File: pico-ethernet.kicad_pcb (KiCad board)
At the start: 2 copper layers, 55 x 22 mm, 28 parts, among them J1 Conn_01x20_Pin, J2 Conn_01x02_Pin, J3 VR05S05, J4 SI-52003-F, J5 Conn_01x02, U1 ENC28J60x-SS, Y1 25MHz

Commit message: interrupt
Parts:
- J2: footprint Connector_PinSocket_2.54mm:PinSocket_1x04_P2.54mm_Vertical -> Connector_PinSocket_2.54mm:PinSocket_1x05_P2.54mm_Vertical
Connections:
- U1 pad 4: unconnected-(U1-~{INT}-Pad4) -> Net-(J2-Pin_5)
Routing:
- net Net-(J2-Pin_5): track 0.00 -> 12.4 mm
- net GND: track 14.2 -> 11.3 mm, vias 4 -> 3

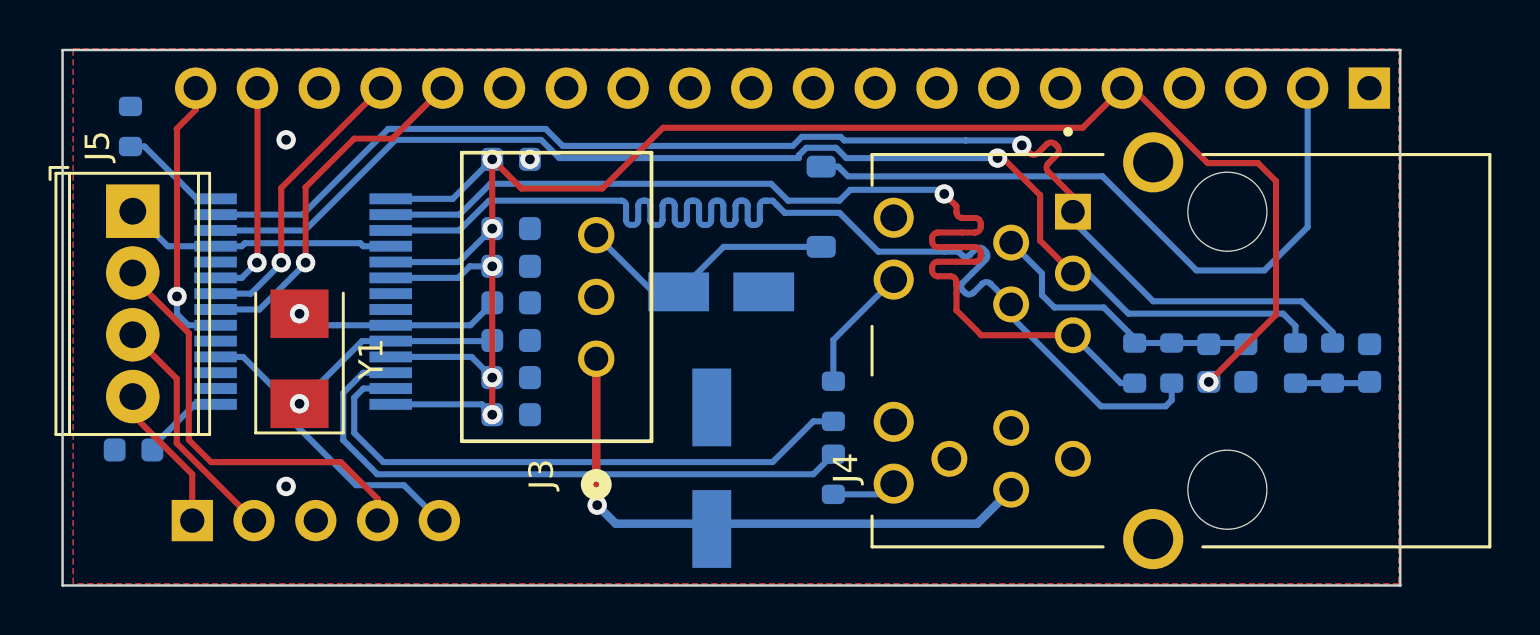
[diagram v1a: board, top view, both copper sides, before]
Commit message: TX RX swap
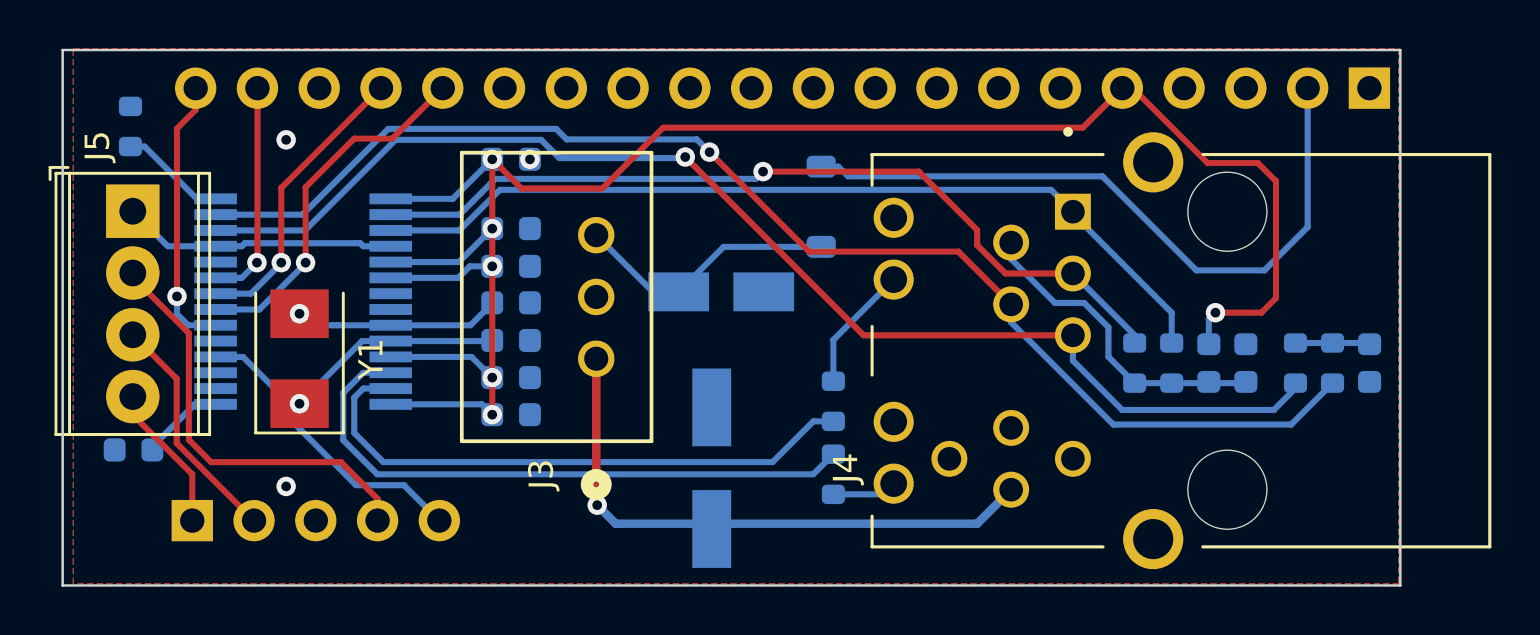
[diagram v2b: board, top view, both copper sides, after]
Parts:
- turned C7 to -90 degrees
- turned C8 to 90 degrees
- turned FB1 to -90 degrees
- turned R2 to 90 degrees
- turned R3 to 90 degrees
- turned R4 to -90 degrees
- turned R5 to -90 degrees
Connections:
- R2 pad 1: Net-(J4-TD-) -> Net-(J4-RD-)
- R3 pad 1: Net-(J4-TD+) -> Net-(J4-RD+)
- R4 pad 1: Net-(J4-RD+) -> Net-(J4-TD+)
- R5 pad 1: Net-(J4-RD-) -> Net-(J4-TD-)
- U1 pad 12: Net-(J4-TD-) -> Net-(J4-RD-)
- U1 pad 13: Net-(J4-TD+) -> Net-(J4-RD+)
- U1 pad 16: Net-(J4-RD-) -> Net-(J4-TD-)
- U1 pad 17: Net-(J4-RD+) -> Net-(J4-TD+)
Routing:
- net Net-(J4-TD+): track 53.7 -> 37.2 mm, vias 1 -> 0
- net Net-(J4-TD-): track 51.3 -> 35.0 mm
- net Net-(J4-RD-): track 44.3 -> 51.8 mm
- net Net-(J4-RD+): track 50.0 -> 53.6 mm, vias 0 -> 1
- net Net-(J4-CT): track 12.1 -> 13.2 mm

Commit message: all good, but looks bad
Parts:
- moved Y1 0.34 mm to (148.7, 122.2)
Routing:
- net GND: track 11.4 -> 13.6 mm
- net +3.3V: track 78.7 -> 80.4 mm, vias 6 -> 4

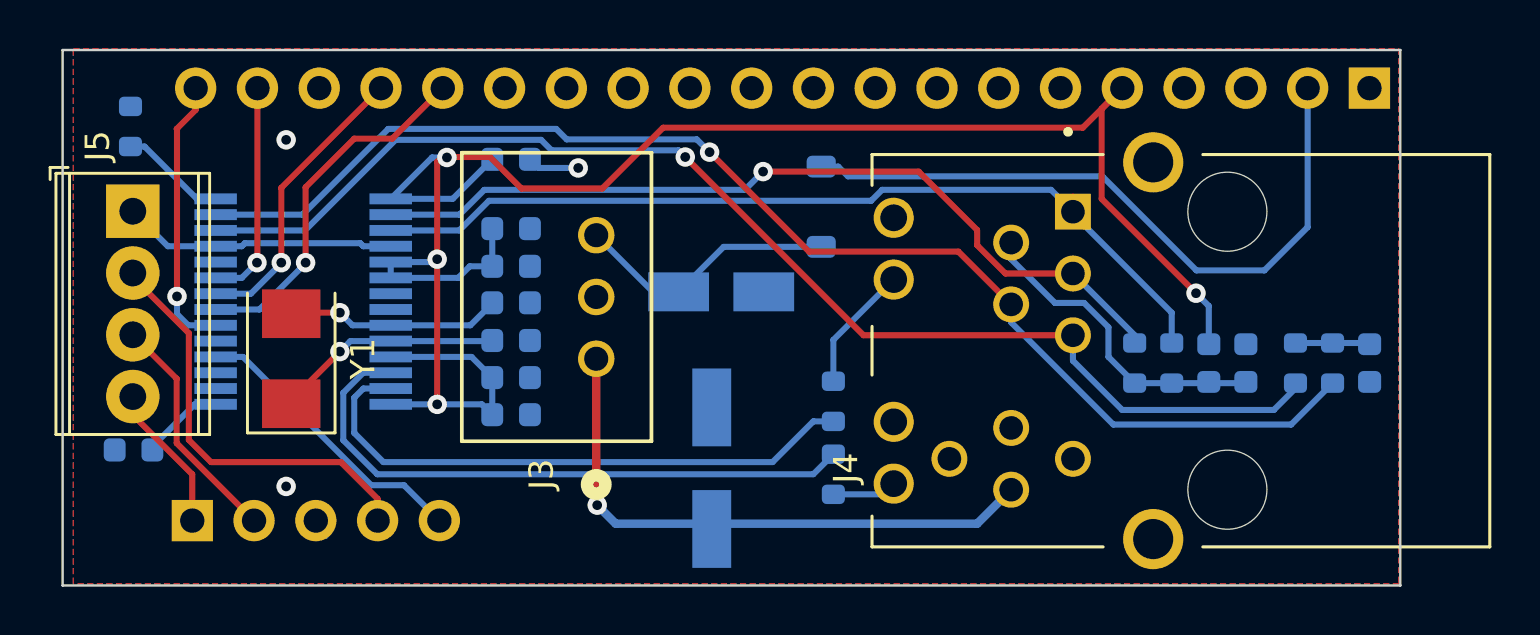
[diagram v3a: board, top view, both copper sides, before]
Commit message: 3v reroute
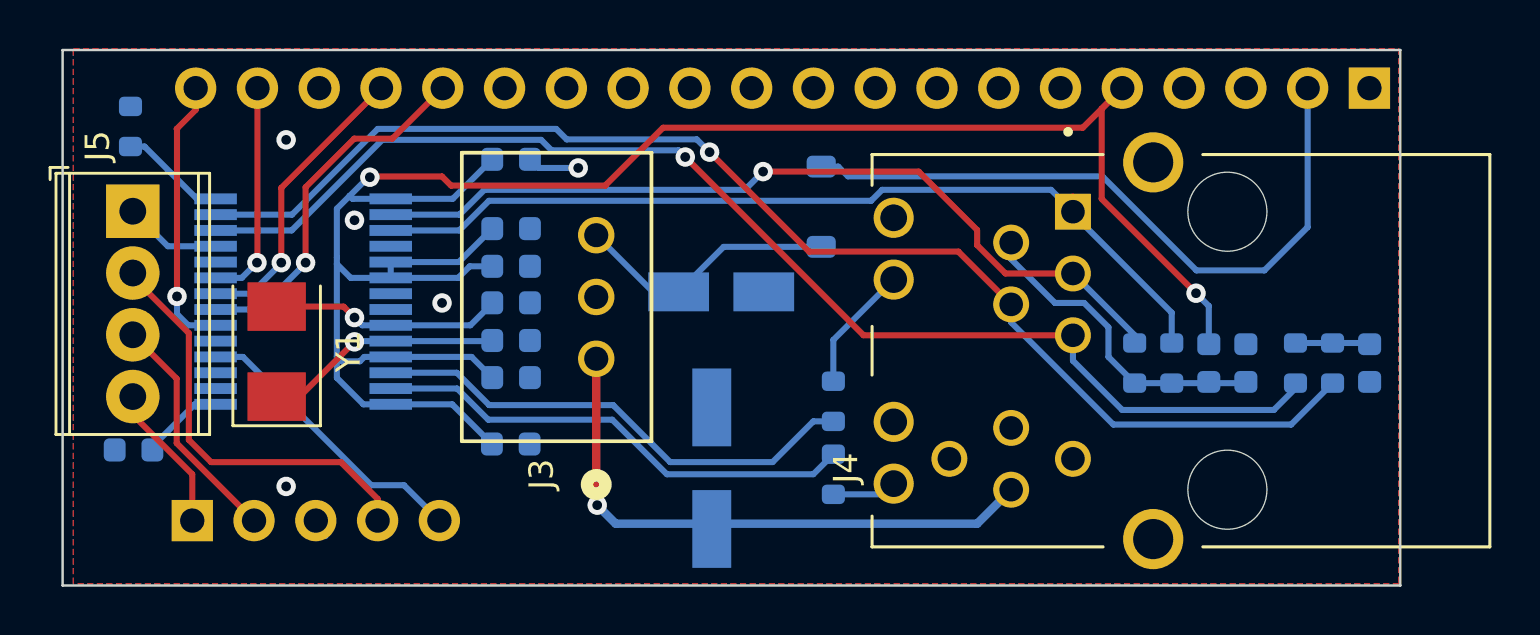
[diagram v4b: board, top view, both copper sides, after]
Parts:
- moved C3 1.21 mm to (157.7, 125.8)
- moved Y1 0.67 mm to (148.1, 122.0)
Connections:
- R6 pad 1: Net-(U1-LEDA) -> Net-(U1-LEDB)
- R7 pad 1: Net-(U1-LEDB) -> Net-(U1-LEDA)
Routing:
- net +3.3V: track 80.4 -> 87.9 mm, vias 4 -> 2
- net GND: track 13.6 -> 6.27 mm, vias 3 -> 5
- net Net-(U1-LEDB): track 25.3 -> 20.6 mm
- net Net-(U1-LEDA): track 24.2 -> 20.0 mm
- net Net-(U1-OSC1): track 8.91 -> 9.59 mm
- net Net-(U1-OSC2): track 9.45 -> 9.99 mm

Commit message: 3v zone
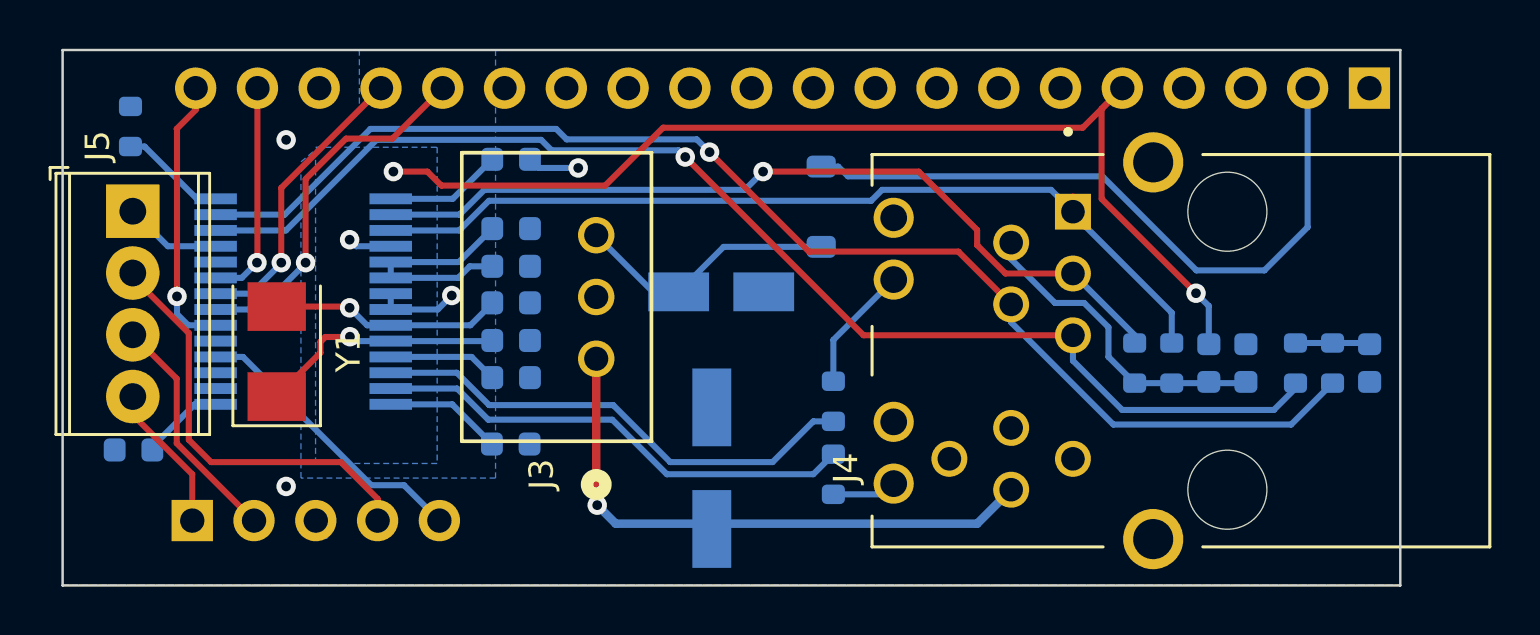
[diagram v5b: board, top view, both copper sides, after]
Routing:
- net +3.3V: track 87.9 -> 68.9 mm
- net GND: track 6.27 -> 11.5 mm
- net Net-(U1-OSC2): track 9.99 -> 11.4 mm
- added copper zone on B.Cu, net +3.3V

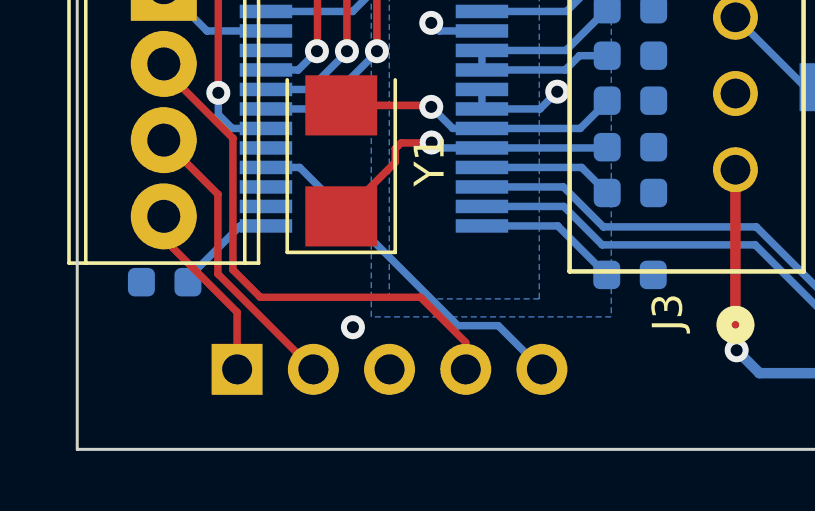
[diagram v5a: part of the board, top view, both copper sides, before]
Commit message: tweak J2 position
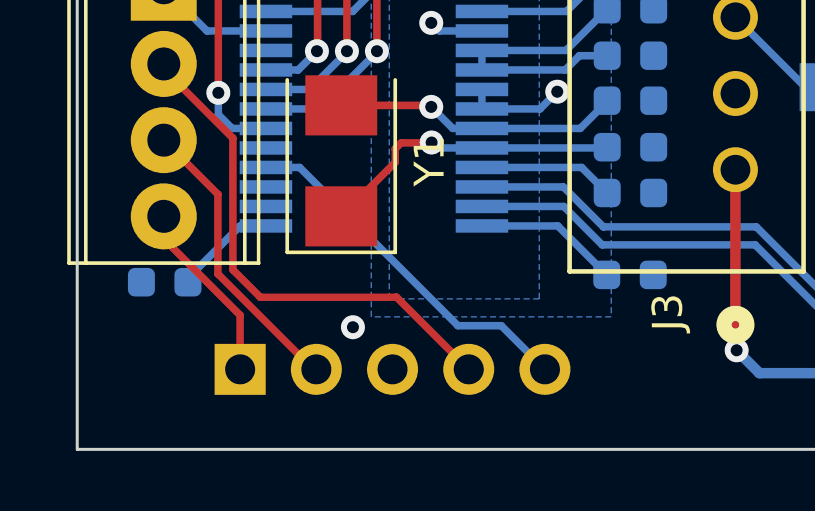
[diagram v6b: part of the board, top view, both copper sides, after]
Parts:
- moved J2 0.10 mm to (144.7, 128.9)
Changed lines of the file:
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@@
 	(footprint "Connector_PinSocket_2.54mm:PinSocket_1x05_P2.54mm_Vertical"
 		(layer "B.Cu")
-		(at 144.64 128.905 -90)
+		(at 144.74 128.905 -90)
 		(descr "Through hole straight socket strip, 1x05, 2.54mm pitch, single row (from Kicad 4.0.7), script generated")
 		(tags "Through hole socket strip THT 1x05 2.54mm single row")
@@
 	)
 	(segment
-		(start 146.725 122.175)
-		(end 152 127.45)
+		(start 145.6 122.175)
+		(end 146.725 122.175)
 		(width 0.25)
 		(layer "B.Cu")
@@
 	)
 	(segment
-		(start 153.345 127.45)
-		(end 154.8 128.905)
+		(start 152 127.45)
+		(end 153.445 127.45)
 		(width 0.25)
 		(layer "B.Cu")
@@
 	)
 	(segment
-		(start 152 127.45)
-		(end 153.345 127.45)
+		(start 153.445 127.45)
+		(end 154.9 128.905)
 		(width 0.25)
 		(layer "B.Cu")
@@
 	)
 	(segment
-		(start 145.6 122.175)
-		(end 146.725 122.175)
+		(start 146.725 122.175)
+		(end 152 127.45)
 		(width 0.25)
 		(layer "B.Cu")
@@
 	)
 	(segment
+		(start 147.18 128.905)
+		(end 147.28 128.905)
+		(width 0.25)
+		(layer "F.Cu")
+		(net 41)
+	)
+	(segment
 		(start 144 123.07)
 		(end 144 125.725)
@@
 	(segment
 		(start 142.195 124.556396)
-		(end 144.64 127.001396)
+		(end 144.74 127.101396)
 		(width 0.25)
 		(layer "F.Cu")
@@
 	)
 	(segment
-		(start 144.64 127.001396)
-		(end 144.64 128.905)
+		(start 144.74 127.101396)
+		(end 144.74 128.905)
 		(width 0.25)
 		(layer "F.Cu")
@@
 	)
 	(segment
-		(start 142.195 118.895)
-		(end 142.195 118.725)
+		(start 145.411396 126.5)
+		(end 144.5 125.588604)
 		(width 0.25)
 		(layer "F.Cu")
@@
 	)
 	(segment
-		(start 152.26 128.905)
-		(end 152.26 128.01)
+		(start 142.195 118.895)
+		(end 142.195 118.725)
 		(width 0.25)
 		(layer "F.Cu")
@@
 	)
 	(segment
-		(start 150.75 126.5)
-		(end 145.411396 126.5)
-		(width 0.25)
-		(layer "F.Cu")
-		(net 43)
-	)
-	(segment
-		(start 144.5 121.2)
-		(end 142.195 118.895)
+		(start 145.411396 126.5)
+		(end 149.955 126.5)
 		(width 0.25)
 		(layer "F.Cu")
@@
 	)
 	(segment
-		(start 152.26 128.01)
-		(end 150.75 126.5)
+		(start 149.955 126.5)
+		(end 152.36 128.905)
 		(width 0.25)
 		(layer "F.Cu")
@@
 	)
 	(segment
-		(start 145.411396 126.5)
-		(end 144.5 125.588604)
+		(start 144.5 121.2)
+		(end 142.195 118.895)
 		(width 0.25)
 		(layer "F.Cu")

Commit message: vanity
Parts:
- added G***: LOGO, LOGO, F.Cu at (167.8, 126.8)
- R6, R7: value 330Ω -> 180Ω

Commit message: unnecessary tuning
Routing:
- net Net-(J4-TD+): track 37.2 -> 48.7 mm
- net Net-(J4-TD-): track 35.0 -> 44.6 mm
- net Net-(J4-RD+): track 53.6 -> 56.0 mm
